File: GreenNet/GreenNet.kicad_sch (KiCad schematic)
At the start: 0 parts

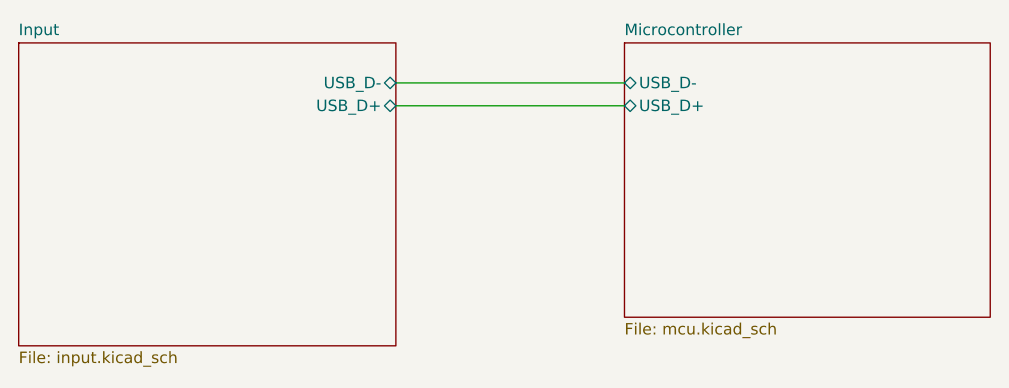
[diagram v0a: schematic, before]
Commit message: finished input schematic
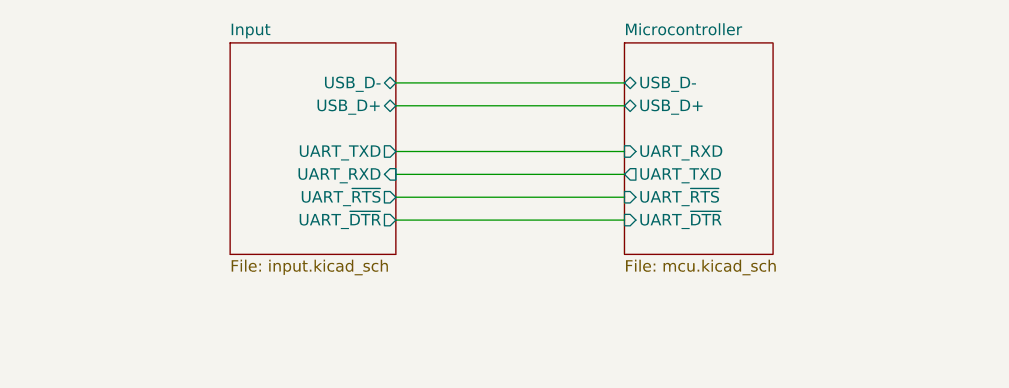
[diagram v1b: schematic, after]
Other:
- sheet Input ports: added UART_RXD, UART_TXD, UART_~{DTR}, UART_~{RTS}; removed none
- sheet Microcontroller ports: added UART_RXD, UART_TXD, UART_~{DTR}, UART_~{RTS}; removed none
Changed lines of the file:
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@@
+	(wire
+		(pts
+			(xy 82.55 80.01) (xy 107.95 80.01)
+		)
+		(stroke
+			(width 0)
+			(type default)
+		)
+	)
 	(wire
 		(pts
 			(xy 82.55 67.31) (xy 107.95 67.31)
+		)
+		(stroke
+			(width 0)
+			(type default)
+		)
+	)
+	(wire
+		(pts
+			(xy 82.55 82.55) (xy 107.95 82.55)
+		)
+		(stroke
+			(width 0)
+			(type default)
+		)
+	)
+	(wire
+		(pts
+			(xy 82.55 74.93) (xy 107.95 74.93)
+		)
+		(stroke
+			(width 0)
+			(type default)
+		)
+	)
+	(wire
+		(pts
+			(xy 82.55 77.47) (xy 107.95 77.47)
 		)
 		(stroke
@@
 	(sheet
 		(at 107.95 62.865)
-		(size 40.64 30.48)
+		(size 16.51 23.495)
 		(fields_autoplaced yes)
 		(stroke
@@
 		)
 		(property "Sheetfile" "mcu.kicad_sch"
-			(at 107.95 93.9296 0)
+			(at 107.95 86.9446 0)
 			(effects
 				(font
@@
 		(pin "USB_D-" bidirectional
 			(at 107.95 67.31 180)
+			(effects
+				(font
+					(size 1.27 1.27)
+				)
+				(justify left)
+			)
+		)
+		(pin "UART_~{RTS}" input
+			(at 107.95 80.01 180)
+			(effects
+				(font
+					(size 1.27 1.27)
+				)
+				(justify left)
+			)
+		)
+		(pin "UART_RXD" input
+			(at 107.95 74.93 180)
+			(effects
+				(font
+					(size 1.27 1.27)
+				)
+				(justify left)
+			)
+		)
+		(pin "UART_TXD" output
+			(at 107.95 77.47 180)
+			(effects
+				(font
+					(size 1.27 1.27)
+				)
+				(justify left)
+			)
+		)
+		(pin "UART_~{DTR}" input
+			(at 107.95 82.55 180)
 			(effects
 				(font
@@
 	)
 	(sheet
-		(at 40.64 62.865)
-		(size 41.91 33.655)
+		(at 64.135 62.865)
+		(size 18.415 23.495)
 		(fields_autoplaced yes)
 		(stroke
@@
 		)
 		(property "Sheetname" "Input"
-			(at 40.64 62.1534 0)
+			(at 64.135 62.1534 0)
 			(effects
 				(font
@@
 		)
 		(property "Sheetfile" "input.kicad_sch"
-			(at 40.64 97.1046 0)
+			(at 64.135 86.9446 0)
 			(effects
 				(font
@@
 			(effects
 				(font
+					(size 1.27 1.27)
+				)
+				(justify right)
+			)
+		)
+		(pin "UART_RXD" input
+			(at 82.55 77.47 0)
+			(effects
+				(font
+					(size 1.27 1.27)
+				)
+				(justify right)
+			)
+		)
+		(pin "UART_~{RTS}" output
+			(at 82.55 80.01 0)
+			(effects
+				(font
+					(size 1.27 1.27)
+				)
+				(justify right)
+			)
+		)
+		(pin "UART_~{DTR}" output
+			(at 82.55 82.55 0)
+			(effects
+				(font
+					(size 1.27 1.27)
+				)
+				(justify right)
+			)
+		)
+		(pin "UART_TXD" output
+			(at 82.55 74.93 0)
+			(effects
+				(font

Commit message: MCU fix
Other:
- added sheet Power (power.kicad_sch)
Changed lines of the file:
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@@
+	)
+	(sheet
+		(at 64.135 101.6)
+		(size 18.415 14.605)
+		(fields_autoplaced yes)
+		(stroke
+			(width 0.1524)
+			(type solid)
+		)
+		(fill
+			(color 0 0 0 0.0000)
+		)
+		(property "Sheetname" "Power"
+			(at 64.135 100.8884 0)
+			(effects
+				(font
+					(size 1.27 1.27)
+				)
+				(justify left bottom)
+			)
+		)
+		(property "Sheetfile" "power.kicad_sch"
+			(at 64.135 116.7896 0)
+			(effects
+				(font
+					(size 1.27 1.27)
+				)
+				(justify left top)
+			)
+		)
+		(instances
+			(project "GreenNet"
+				(path "/189669a5-f2fc-4cde-9413-8df80c557655"
+					(page "4")
+				)
+			)
+		)
 	)
 	(sheet

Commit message: more sensor work
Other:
- added sheet Sensors (sensors.kicad_sch)
- sheet Input ports: added USB_PD_GPIO, USB_PD_INT, USB_PD_SCL, USB_PD_SDA; removed none
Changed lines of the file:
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@@
+	)
+	(sheet
+		(at 69.85 123.19)
+		(size 18.415 14.605)
+		(fields_autoplaced yes)
+		(stroke
+			(width 0.1524)
+			(type solid)
+		)
+		(fill
+			(color 0 0 0 0.0000)
+		)
+		(property "Sheetname" "Sensors"
+			(at 69.85 122.4784 0)
+			(effects
+				(font
+					(size 1.27 1.27)
+				)
+				(justify left bottom)
+			)
+		)
+		(property "Sheetfile" "sensors.kicad_sch"
+			(at 69.85 138.3796 0)
+			(effects
+				(font
+					(size 1.27 1.27)
+				)
+				(justify left top)
+			)
+		)
+		(instances
+			(project "GreenNet"
+				(path "/189669a5-f2fc-4cde-9413-8df80c557655"
+					(page "5")
+				)
+			)
+		)
 	)
 	(sheet
 		(at 107.95 62.865)
-		(size 16.51 23.495)
+		(size 16.51 35.56)
 		(fields_autoplaced yes)
 		(stroke
@@
 		)
 		(property "Sheetfile" "mcu.kicad_sch"
-			(at 107.95 86.9446 0)
+			(at 107.95 99.0096 0)
 			(effects
 				(font
@@
 	)
 	(sheet
-		(at 64.135 101.6)
+		(at 34.925 120.65)
 		(size 18.415 14.605)
 		(fields_autoplaced yes)
@@
 		)
 		(property "Sheetname" "Power"
-			(at 64.135 100.8884 0)
+			(at 34.925 119.9384 0)
 			(effects
 				(font
@@
 		)
 		(property "Sheetfile" "power.kicad_sch"
-			(at 64.135 116.7896 0)
+			(at 34.925 135.8396 0)
 			(effects
 				(font
@@
 	(sheet
 		(at 64.135 62.865)
-		(size 18.415 23.495)
+		(size 18.415 36.195)
 		(fields_autoplaced yes)
 		(stroke
@@
 		)
 		(property "Sheetfile" "input.kicad_sch"
-			(at 64.135 86.9446 0)
+			(at 64.135 99.6446 0)
 			(effects
 				(font
@@
 			(effects
 				(font
+					(size 1.27 1.27)
+				)
+				(justify right)
+			)
+		)
+		(pin "USB_PD_GPIO" bidirectional
+			(at 82.55 95.25 0)
+			(effects
+				(font
+					(size 1.27 1.27)
+				)
+				(justify right)
+			)
+		)
+		(pin "USB_PD_SCL" bidirectional
+			(at 82.55 90.17 0)
+			(effects
+				(font
+					(size 1.27 1.27)
+				)
+				(justify right)
+			)
+		)
+		(pin "USB_PD_SDA" bidirectional
+			(at 82.55 87.63 0)
+			(effects
+				(font
+					(size 1.27 1.27)
+				)
+				(justify right)
+			)
+		)
+		(pin "USB_PD_INT" output
+			(at 82.55 92.71 0)
+			(effects
+				(font

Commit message: significant progress
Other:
- sheet Sensors renamed Peripherals
- sheet Input ports: added PWR_SCL, PWR_SDA; removed USB_PD_SCL, USB_PD_SDA
- sheet Microcontroller ports: added BAT_EN1, BAT_EN2, BAT_INT, BAT_~{CE}, LCD_EN, LTR_INT, PERI_SCL, PERI_SDA, PWR_SCL, PWR_SDA, SOIL_EN, SOIL_SENSE, USB_PD_GPIO, USB_PD_INT; removed none
- sheet Peripherals: file sensors.kicad_sch -> peripherals.kicad_sch
- sheet Peripherals ports: added LCD_EN, LTR_INT, PERI_SCL, PERI_SDA, SOIL_EN, SOIL_SENSE; removed none
- sheet Power ports: added BAT_EN1, BAT_EN2, BAT_INT, BAT_~{CE}, PWR_SCL, PWR_SDA; removed none

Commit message: update
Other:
- removed sheet Peripherals
- removed sheet Power
- sheet Input ports: added none; removed PWR_SCL, PWR_SDA, USB_PD_GPIO, USB_PD_INT
- sheet Microcontroller ports: added none; removed BAT_EN1, BAT_EN2, BAT_INT, BAT_~{CE}, PWR_SCL, PWR_SDA, USB_PD_GPIO, USB_PD_INT

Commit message: schematic FINAL
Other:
- sheet Input ports: added LTR_INT, PERI_SCL, PERI_SDA, SOIL_EN, SOIL_SENSE; removed none
- sheet Microcontroller ports: added none; removed LCD_EN
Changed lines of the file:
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@@
 	(wire
 		(pts
-			(xy 95.25 80.01) (xy 107.95 80.01)
-		)
-		(stroke
-			(width 0)
-			(type default)
-		)
-	)
-	(wire
-		(pts
-			(xy 95.25 67.31) (xy 107.95 67.31)
-		)
-		(stroke
-			(width 0)
-			(type default)
-		)
-	)
-	(wire
-		(pts
-			(xy 95.25 82.55) (xy 107.95 82.55)
-		)
-		(stroke
-			(width 0)
-			(type default)
-		)
-	)
-	(wire
-		(pts
-			(xy 95.25 74.93) (xy 107.95 74.93)
-		)
-		(stroke
-			(width 0)
-			(type default)
-		)
-	)
-	(wire
-		(pts
-			(xy 95.25 77.47) (xy 107.95 77.47)
-		)
-		(stroke
-			(width 0)
-			(type default)
-		)
-	)
-	(wire
-		(pts
-			(xy 95.25 69.85) (xy 107.95 69.85)
+			(xy 137.16 115.57) (xy 149.86 115.57)
+		)
+		(stroke
+			(width 0)
+			(type default)
+		)
+	)
+	(wire
+		(pts
+			(xy 137.16 107.95) (xy 149.86 107.95)
+		)
+		(stroke
+			(width 0)
+			(type default)
+		)
+	)
+	(wire
+		(pts
+			(xy 137.16 113.03) (xy 149.86 113.03)
+		)
+		(stroke
+			(width 0)
+			(type default)
+		)
+	)
+	(wire
+		(pts
+			(xy 137.16 97.79) (xy 149.86 97.79)
+		)
+		(stroke
+			(width 0)
+			(type default)
+		)
+	)
+	(wire
+		(pts
+			(xy 137.16 85.09) (xy 149.86 85.09)
+		)
+		(stroke
+			(width 0)
+			(type default)
+		)
+	)
+	(wire
+		(pts
+			(xy 137.16 100.33) (xy 149.86 100.33)
+		)
+		(stroke
+			(width 0)
+			(type default)
+		)
+	)
+	(wire
+		(pts
+			(xy 137.16 105.41) (xy 149.86 105.41)
+		)
+		(stroke
+			(width 0)
+			(type default)
+		)
+	)
+	(wire
+		(pts
+			(xy 137.16 92.71) (xy 149.86 92.71)
+		)
+		(stroke
+			(width 0)
+			(type default)
+		)
+	)
+	(wire
+		(pts
+			(xy 137.16 95.25) (xy 149.86 95.25)
+		)
+		(stroke
+			(width 0)
+			(type default)
+		)
+	)
+	(wire
+		(pts
+			(xy 137.16 87.63) (xy 149.86 87.63)
+		)
+		(stroke
+			(width 0)
+			(type default)
+		)
+	)
+	(wire
+		(pts
+			(xy 137.16 118.11) (xy 149.86 118.11)
 		)
 		(stroke
@@
 	)
 	(sheet
-		(at 107.95 64.135)
-		(size 29.21 62.23)
+		(at 149.86 82.55)
+		(size 29.21 38.1)
 		(fields_autoplaced yes)
 		(stroke
@@
 		)
 		(property "Sheetname" "Microcontroller"
-			(at 107.95 63.4234 0)
+			(at 149.86 81.8384 0)
 			(effects
 				(font
@@
 		)
 		(property "Sheetfile" "mcu.kicad_sch"
-			(at 107.95 126.9496 0)
+			(at 149.86 121.2346 0)
 			(effects
 				(font
@@
 		)
 		(pin "USB_D+" bidirectional
-			(at 107.95 69.85 180)
+			(at 149.86 87.63 180)
 			(effects
 				(font
@@
 		)
 		(pin "USB_D-" bidirectional
-			(at 107.95 67.31 180)
+			(at 149.86 85.09 180)
 			(effects
 				(font
@@
 		)
 		(pin "UART_~{RTS}" input
-			(at 107.95 80.01 180)
+			(at 149.86 97.79 180)
 			(effects
 				(font
@@
 		)
 		(pin "UART_RXD" input
-			(at 107.95 74.93 180)
+			(at 149.86 92.71 180)
 			(effects
 				(font
@@
 		)
 		(pin "UART_TXD" output
-			(at 107.95 77.47 180)
+			(at 149.86 95.25 180)
 			(effects
 				(font
@@
 		)
 		(pin "UART_~{DTR}" input
-			(at 107.95 82.55 180)
+			(at 149.86 100.33 180)
 			(effects
 				(font
@@
 		)
 		(pin "PERI_SDA" bidirectional
-			(at 137.16 67.31 0)
-			(effects
-				(font
-					(size 1.27 1.27)
-				)
-				(justify right)
+			(at 149.86 105.41 180)
+			(effects
+				(font
+					(size 1.27 1.27)
+				)
+				(justify left)
 			)
 		)
 		(pin "PERI_SCL" bidirectional
-			(at 137.16 69.85 0)
-			(effects
-				(font
-					(size 1.27 1.27)
-				)
-				(justify right)
+			(at 149.86 107.95 180)
+			(effects
+				(font
+					(size 1.27 1.27)
+				)
+				(justify left)
 			)
 		)
 		(pin "SOIL_SENSE" input
-			(at 137.16 82.55 0)
-			(effects
-				(font
-					(size 1.27 1.27)
-				)
-				(justify right)
+			(at 149.86 115.57 180)
+			(effects
+				(font
+					(size 1.27 1.27)
+				)
+				(justify left)
 			)
 		)
 		(pin "SOIL_EN" output
-			(at 137.16 74.93 0)
-			(effects
-				(font
-					(size 1.27 1.27)
-				)
-				(justify right)
+			(at 149.86 118.11 180)
+			(effects
+				(font
+					(size 1.27 1.27)
+				)
+				(justify left)
 			)
 		)
 		(pin "LTR_INT" input
-			(at 137.16 77.47 0)
-			(effects
-				(font
-					(size 1.27 1.27)
-				)
-				(justify right)
-			)
-		)
-		(pin "LCD_EN" output
-			(at 137.16 80.01 0)
-			(effects
-				(font
-					(size 1.27 1.27)
-				)
-				(justify right)
+			(at 149.86 113.03 180)
+			(effects
+				(font
+					(size 1.27 1.27)
+				)
+				(justify left)
 			)
 		)
@@
 	)
 	(sheet
-		(at 74.93 64.77)
-		(size 20.32 33.02)
+		(at 116.84 82.55)
+		(size 20.32 38.1)
 		(fields_autoplaced yes)
 		(stroke
@@
 		)
 		(property "Sheetname" "Input"
-			(at 74.93 64.0584 0)
+			(at 116.84 81.8384 0)
 			(effects
 				(font
@@
 		)
 		(property "Sheetfile" "input.kicad_sch"
-			(at 74.93 98.3746 0)
+			(at 116.84 121.2346 0)
 			(effects
 				(font
@@
 		)
 		(pin "USB_D-" bidirectional
-			(at 95.25 67.31 0)
+			(at 137.16 85.09 0)
 			(effects
 				(font
@@
 		)
 		(pin "USB_D+" bidirectional
-			(at 95.25 69.85 0)
+			(at 137.16 87.63 0)
 			(effects
 				(font
@@
 		)
 		(pin "UART_RXD" input
-			(at 95.25 77.47 0)
+			(at 137.16 95.25 0)
 			(effects
 				(font
@@
 		)
 		(pin "UART_~{RTS}" output
-			(at 95.25 80.01 0)
+			(at 137.16 97.79 0)
 			(effects
 				(font
@@
 		)
 		(pin "UART_~{DTR}" output
-			(at 95.25 82.55 0)
+			(at 137.16 100.33 0)
 			(effects
 				(font
@@
 		)
 		(pin "UART_TXD" output
-			(at 95.25 74.93 0)
-			(effects
-				(font
+			(at 137.16 92.71 0)
+			(effects
+				(font
+					(size 1.27 1.27)
+				)
+				(justify right)
+			)
+		)
+		(pin "SOIL_EN" input
+			(at 137.16 118.11 0)
+			(effects
+				(font
+					(size 1.27 1.27)
+				)
+				(justify right)
+			)
+		)
+		(pin "SOIL_SENSE" output
+			(at 137.16 115.57 0)
+			(effects
+				(font
+					(size 1.27 1.27)
+				)
+				(justify right)
+			)
+		)
+		(pin "LTR_INT" output
+			(at 137.16 113.03 0)
+			(effects
+				(font
+					(size 1.27 1.27)
+				)
+				(justify right)
+			)
+		)
+		(pin "PERI_SDA" bidirectional
+			(at 137.16 105.41 0)
+			(effects
+				(font
+					(size 1.27 1.27)
+				)
+				(justify right)
+			)
+		)
+		(pin "PERI_SCL" bidirectional
+			(at 137.16 107.95 0)
+			(effects
+				(font
